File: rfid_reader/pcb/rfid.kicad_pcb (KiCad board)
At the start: 2 copper layers, 25 parts, among them IC1 ATMEGA8-P, P1 CONN_2, P2 CONN_4, P3 CONN_2, Q1 BS107, Q2 BC547, U1 LM358, X1 8MHz

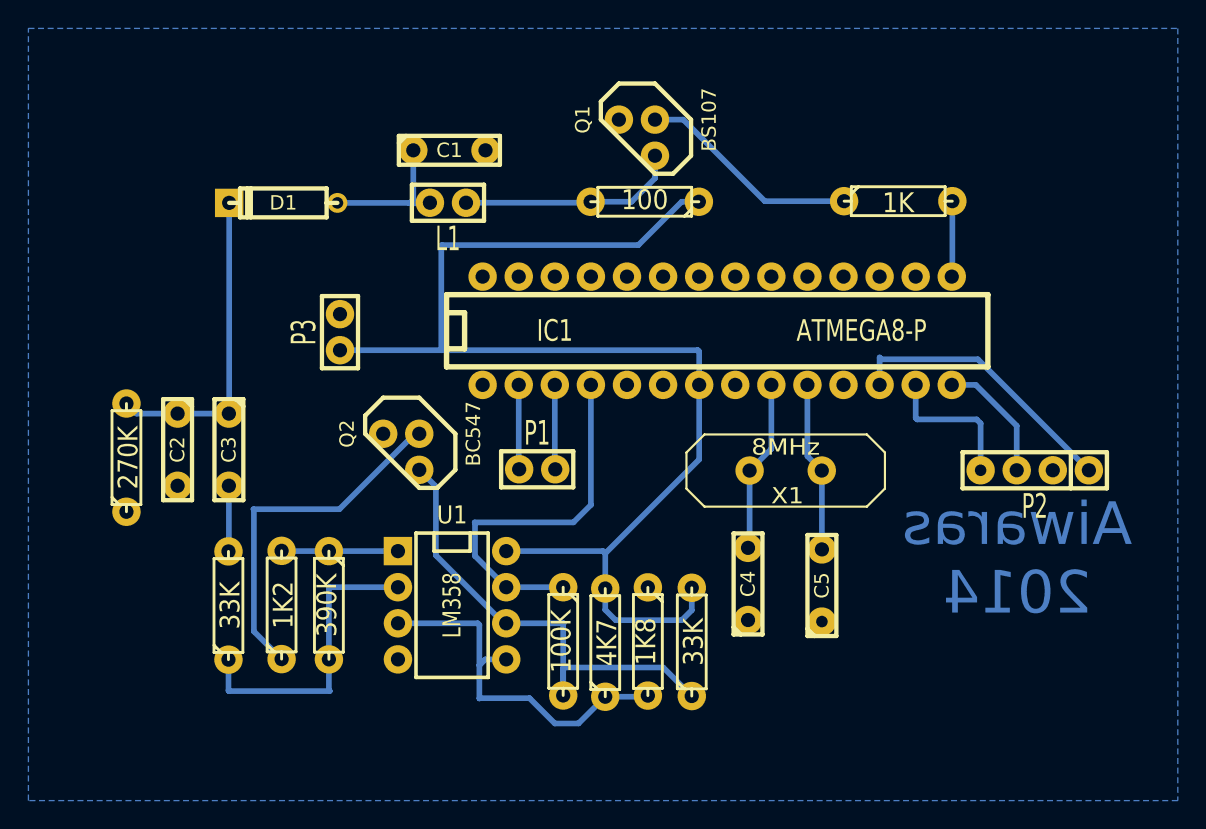
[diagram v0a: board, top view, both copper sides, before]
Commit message: Added I2C to PSB
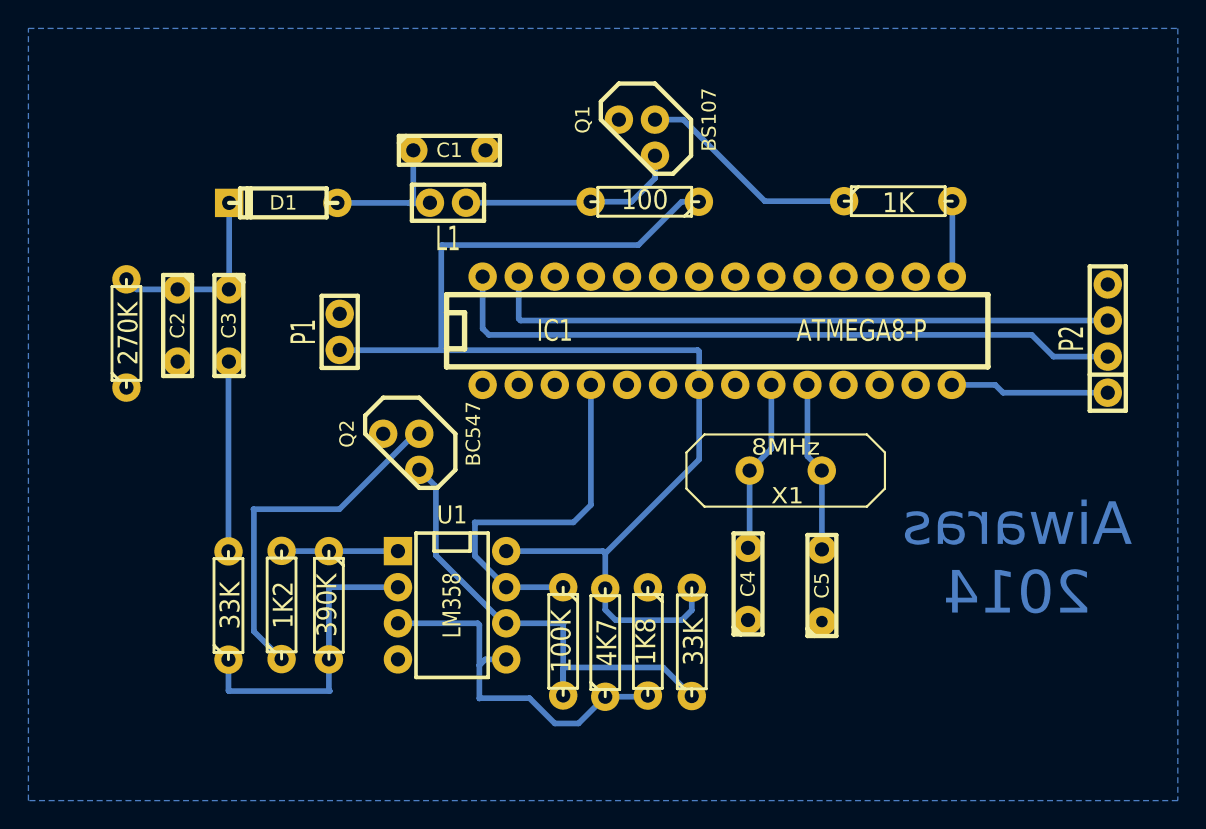
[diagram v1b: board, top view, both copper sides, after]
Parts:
- removed P3: CONN_2, SIL-2
- moved P1 16.9 mm to (77.9, 83.0), turned to 90 degrees
- moved P2 10.6 mm to (132.0, 83.4), turned to 90 degrees
- moved R3 8.74 mm to (62.9, 83.1)
- moved C2 8.74 mm to (66.5, 82.5)
- moved C3 8.74 mm to (70.1, 82.5)
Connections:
- IC1 pad 12: N-0000010 -> (no net)
- IC1 pad 13: N-0000012 -> (no net)
- IC1 pad 14: N-0000011 -> N-0000010
- IC1 pad 2: N-0000015 -> (no net)
- IC1 pad 27: (no net) -> N-0000011
- IC1 pad 28: (no net) -> N-0000012
- IC1 pad 3: N-0000014 -> (no net)
- P1 pad 1: N-0000015 -> +5V
- P1 pad 2: N-0000014 -> GND
- P2 pad 2: GND -> N-0000012
- P2 pad 4: N-0000012 -> GND
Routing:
- net N-0000012: track 10.4 -> 48.5 mm
- net N-0000011: track 8.89 -> 44.5 mm
- net N-0000032: track 4.63 -> 13.4 mm
- net N-0000010: track 19.9 -> 11.2 mm
- net N-0000038: track 22.3 -> 13.6 mm
- net N-0000015: track 5.95 -> 0.00 mm
- net N-0000014: track 5.95 -> 0.00 mm
